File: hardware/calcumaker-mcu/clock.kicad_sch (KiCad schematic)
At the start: 3 parts, among them Y1 32.768kHz

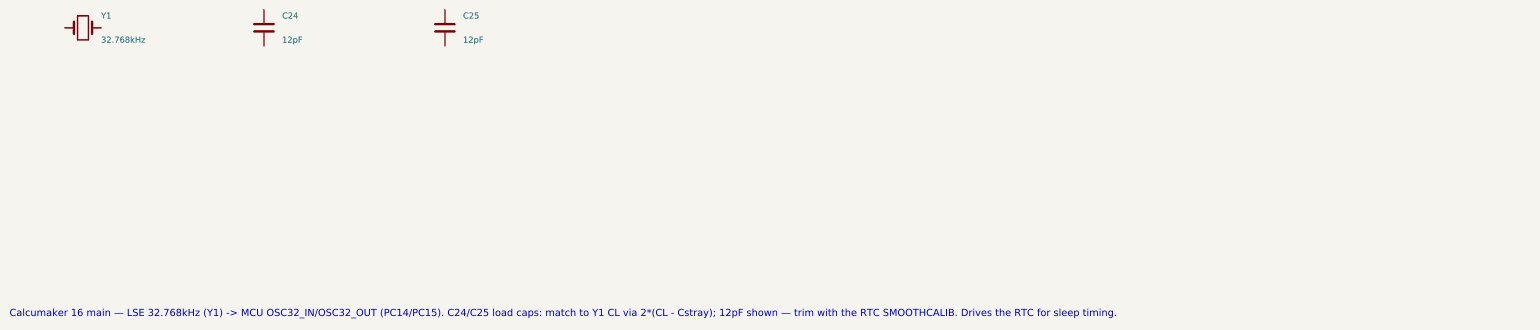
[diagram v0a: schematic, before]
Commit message: hardware: 3-board split (MCU + keyboard + display), wired display, real connectors (#1)
* hardware: 3-board split (MCU + keyboard + display), wired display, real connectors

Split the single logic board into three, wire the display as a KiCad
multi-channel design, and settle every interconnect on real, in-stock parts.

Three-board split (was two):
- Rename calcumaker-main -> calcumaker-mcu (brain/PSU logic board).
- New calcumaker-keyboard board: 50-key Cherry MX matrix + its own
  STM32G031K8U6 scanner (LCSC C432207, UFQFPN-32) + annunciator LEDs,
  mezzanine-stacked above the MCU board. Keyscanning is off the main board;
  only an I2C + UART link + KB_IRQ wake + power cross the mezzanine.

Display board (calcumaker-display):
- Corrected FJ5161AH to a SINGLE-digit 0.56" common-cathode part (C8093) --
  it is NOT a 4-digit module; 48 single digits (16/row x 3), authored symbol
  + 0.56" LTS6760 land. The old 4-digit CC56-12 mapping (and its 3D model)
  was the phantom "clock colon".
- Rebuilt as a KiCad multi-channel design: one reusable display_row.kicad_sch
  (1 TM1640 + 16 digits, fully wired) instantiated x3. Extended kschgen.py
  with wiring primitives + reused-sheet (multi-channel) support.

Connectors (real, verified LCSC / DigiKey parts):
- Display link -> 0.5mm 12P FFC: AFC01-S12FCA-00 (LCSC C262661) on both
  boards; cable = GCT FFC05-TIN 05-12-A-<len>-A-4-06-4-T (DigiKey accessory,
  length TBD). +5V/GND conductors doubled for the display LED current.
- Keyboard mezzanine -> low-profile Hirose DF40 (0.4mm, 2x5, 1.5mm stack):
  DF40C-10DS (C424636) + DF40C-10DP (C424635) -- dedicated KiCad footprint
  + 3D model, unlike the datasheet-less generic parts first considered.

Low-power & wake documented (two Stop domains; keypress -> G0 EXTI wake ->
KB_IRQ -> U575 WKUP; G0 also wakes on I2C address-match). calcumaker-core
is unchanged -- App still consumes (row,col).

All three boards generate + pass the structure check (mcu 52 / keyboard 119 /
display 60 compo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
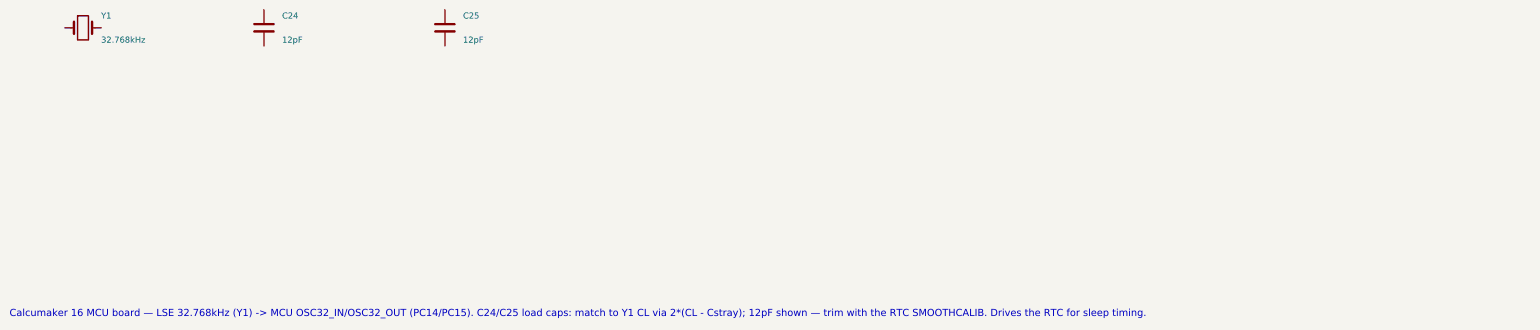
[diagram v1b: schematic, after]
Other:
- note added: "Calcumaker 16 MCU board — LSE 32.768kHz (Y1) -> MCU OSC32_IN/OSC32_OUT (PC14/PC15). C24/C25 load caps: match to Y1 CL via 2*(CL - Cstray); 12pF shown — trim with the RTC SMOOTHCALIB. Drives the RTC for sleep timing."
- note removed: "Calcumaker 16 main — LSE 32.768kHz (Y1) -> MCU OSC32_IN/OSC32_OUT (PC14/PC15). C24/C25 load caps: match to Y1 CL via 2*(CL - Cstray); 12pF shown — trim with the RTC SMOOTHCALIB. Drives the RTC for sleep timing."
- title: Calcumaker 16 — Main — LSE 32.768 kHz (RTC) -> Calcumaker 16 — MCU — LSE 32.768 kHz (RTC)
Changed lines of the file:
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@@
 	(paper "A3")
 	(title_block
-		(title "Calcumaker 16 — Main — LSE 32.768 kHz (RTC)")
-		(date "2026-06-21")
-		(rev "0.1")
+		(title "Calcumaker 16 — MCU — LSE 32.768 kHz (RTC)")
+		(date "2026-07-05")
+		(rev "0.2")
 		(company "calcumaker authors")
 	)
@@
 		(pin "2")
 		(instances
-			(project "calcumaker-main"
-				(path "/ca1c0000-0000-4000-8000-00000000ma01/4dd16969-fa48-40a9-bf37-e7180cf6be85"
+			(project "calcumaker-mcu"
+				(path "/ca1c0000-0000-4000-8000-00000000ma01/dc502c7f-271d-4dc5-a1c2-d18857eddfee"
 					(reference "Y1")
 					(unit 1)
@@
 		(pin "2")
 		(instances
-			(project "calcumaker-main"
-				(path "/ca1c0000-0000-4000-8000-00000000ma01/4dd16969-fa48-40a9-bf37-e7180cf6be85"
+			(project "calcumaker-mcu"
+				(path "/ca1c0000-0000-4000-8000-00000000ma01/dc502c7f-271d-4dc5-a1c2-d18857eddfee"
 					(reference "C24")
 					(unit 1)
@@
 		(pin "2")
 		(instances
-			(project "calcumaker-main"
-				(path "/ca1c0000-0000-4000-8000-00000000ma01/4dd16969-fa48-40a9-bf37-e7180cf6be85"
+			(project "calcumaker-mcu"
+				(path "/ca1c0000-0000-4000-8000-00000000ma01/dc502c7f-271d-4dc5-a1c2-d18857eddfee"
 					(reference "C25")
 					(unit 1)
@@
 		)
 	)
-	(text "Calcumaker 16 main — LSE 32.768kHz (Y1) -> MCU OSC32_IN/OSC32_OUT (PC14/PC15). C24/C25 load caps: match to Y1 CL via 2*(CL - Cstray); 12pF shown — trim with the RTC SMOOTHCALIB. Drives the RTC for sleep timing."
+	(text "Calcumaker 16 MCU board — LSE 32.768kHz (Y1) -> MCU OSC32_IN/OSC32_OUT (PC14/PC15). C24/C25 load caps: match to Y1 CL via 2*(CL - Cstray); 12pF shown — trim with the RTC SMOOTHCALIB. Drives the RTC for sleep timing."
 		(exclude_from_sim no)
 		(at 15.00 100.00 0)
